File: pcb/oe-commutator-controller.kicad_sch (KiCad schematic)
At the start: 57 parts, among them J1 1719730004, U1 TEENSY-LC, U2 IS31FL3193, U3 TMC2130-LA, U4 PTN04050CAZ, U5 LTC4425

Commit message: Board revision C
- Sent to JLCPCB for testing
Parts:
- C11, C17, C6: value 2.2uF -> 4.7uF
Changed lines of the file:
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@@
       (effects (font (size 1.27 1.27)) (justify left))
     )
-    (property "Value" "2.2uF" (at 26.67 138.43 0)
+    (property "Value" "4.7uF" (at 26.67 138.43 0)
       (effects (font (size 1.27 1.27)) (justify left))
     )
@@
       (effects (font (size 1.27 1.27)) (justify left))
     )
-    (property "Value" "2.2uF" (at 151.13 41.91 0)
+    (property "Value" "4.7uF" (at 151.13 41.91 0)
       (effects (font (size 1.27 1.27)) (justify left))
     )
@@
       (effects (font (size 1.27 1.27)) (justify left))
     )
-    (property "Value" "2.2uF" (at 182.88 74.93 0)
+    (property "Value" "4.7uF" (at 182.88 74.93 0)
       (effects (font (size 1.27 1.27)) (justify left))
     )
@@
       (effects (font (size 1.27 1.27)) hide)
     )
-    (property "Datasheet" "~" (at 110.49 46.99 0)
-      (effects (font (size 1.27 1.27)) hide)
-    )
+    (property "Datasheet" "https://www.sunledusa.com/products/spec/XZMDKCBDDG45S-9.pdf" (at 110.49 46.99 0)
+      (effects (font (size 1.27 1.27)) hide)
+    )

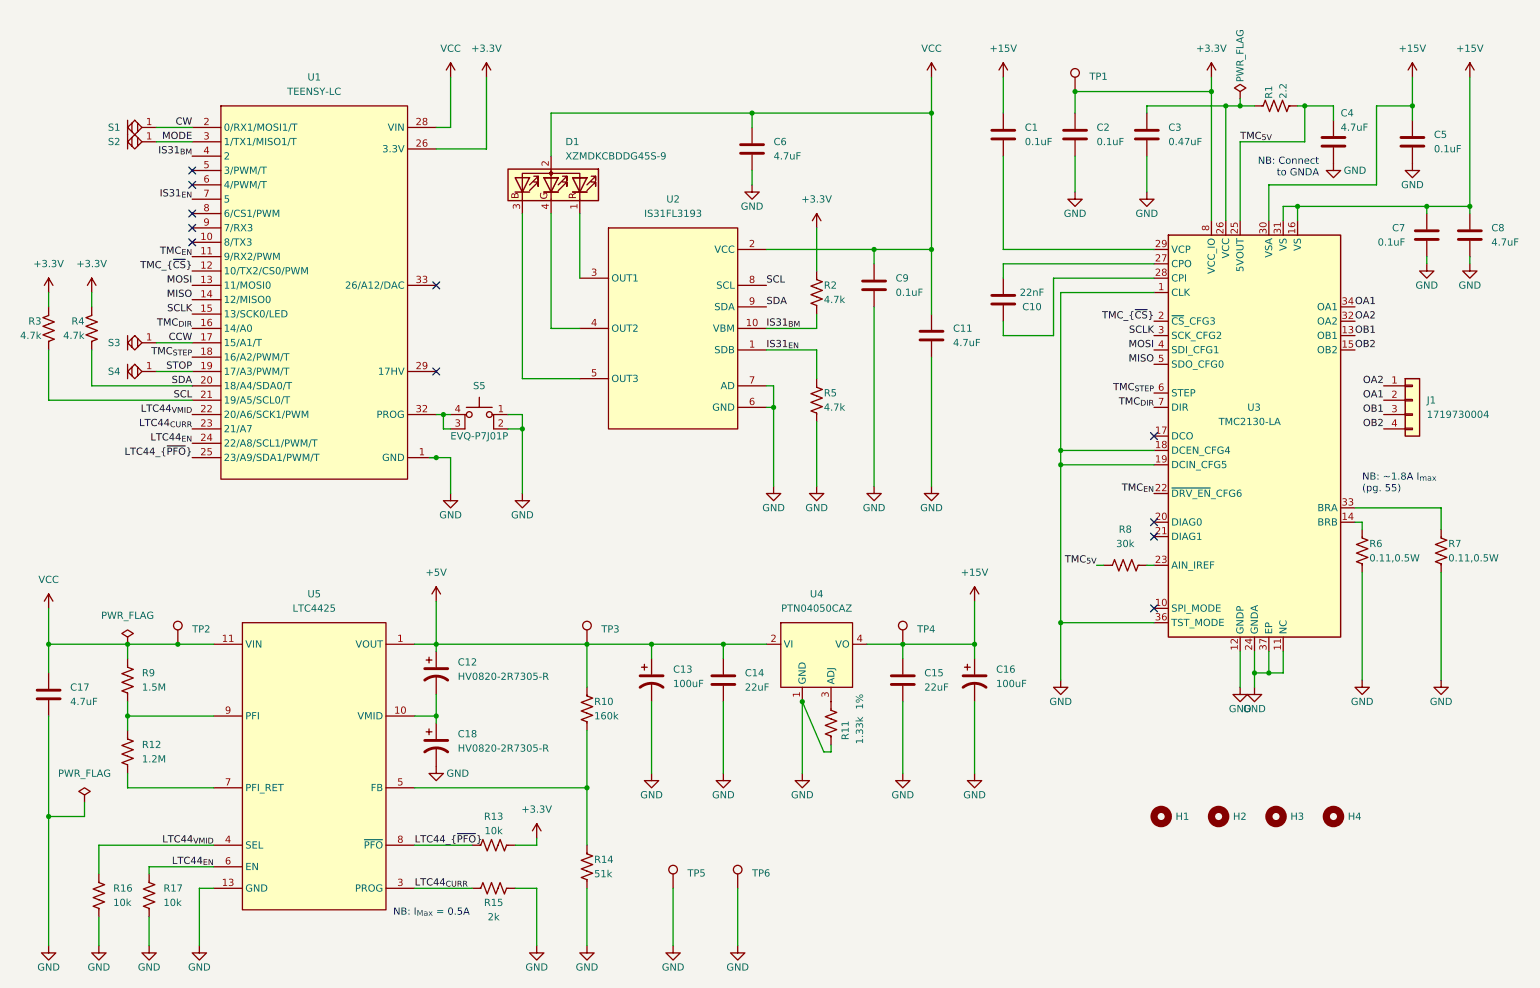
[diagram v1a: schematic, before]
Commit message: Increase R_prog to 2.49k
- This accounts for overhead current drawn from VCC by the Teensy and
  LED driver
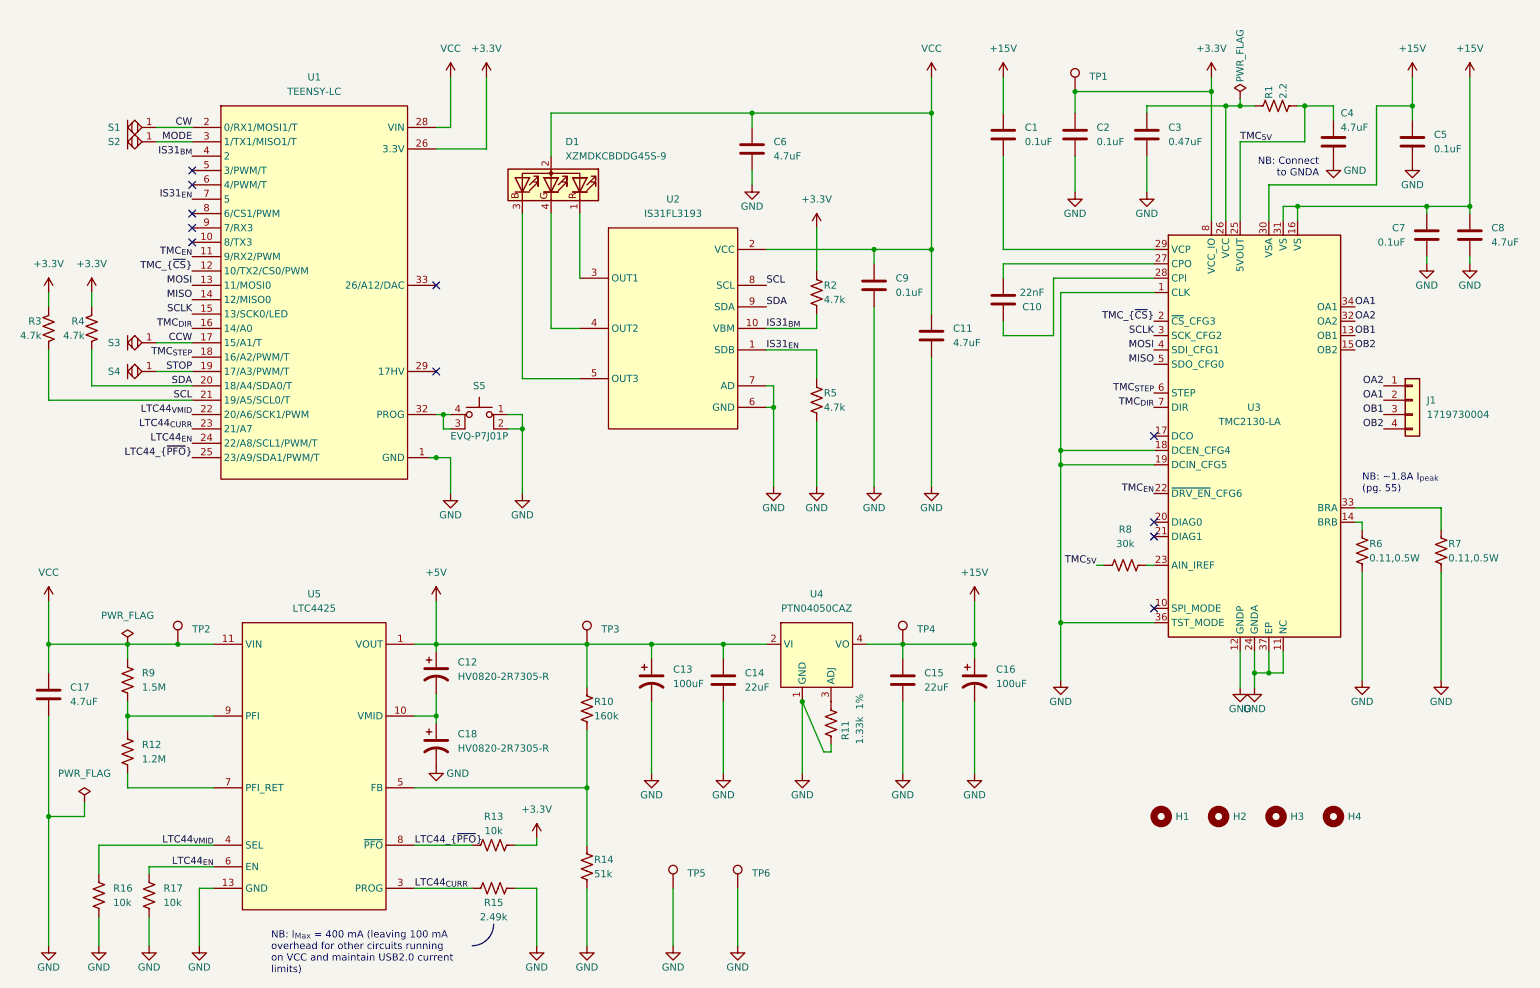
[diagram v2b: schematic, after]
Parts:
- R15: value 2k -> 2.49k
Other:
- note added: "NB: I_{Max} = 400 mA (leaving 100 mA overhead for other circuits running on VCC and maintain USB2.0 current limits)"
- note added: "NB: ~1.8A I_{peak} (pg. 55)"
- note removed: "NB: I_{Max} = 0.5A"
- note removed: "NB: ~1.8A I_{max} (pg. 55)"
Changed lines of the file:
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@@
     (stroke (width 0) (type default))
   )
-  (wire (pts (xy 22.86 121.92) (xy 22.86 128.27))
+  (wire (pts (xy 22.86 120.65) (xy 22.86 128.27))
     (stroke (width 0) (type default))
   )
@@
     (stroke (width 0) (type default))
   )
-  (text "NB: ~1.8A I_{max}\n(pg. 55)" (at 255.27 101.6 0)
+  (arc (start 101.6 177.8) (mid 100.4841 180.4941) (end 97.79 181.61)
+    (stroke (width 0) (type default))
+    (fill (type none))
+  )
+  (text "NB: ~1.8A I_{peak}\n(pg. 55)" (at 255.27 101.6 0)
     (effects (font (size 1.27 1.27)) (justify left bottom))
   )
-  (text "NB: I_{Max} = 0.5A" (at 83.82 176.53 0)
+  (text "NB: I_{Max} = 400 mA (leaving 100 mA \noverhead for other circuits running \non VCC and maintain USB2.0 current \nlimits)"
+    (at 62.23 186.69 0)
     (effects (font (size 1.27 1.27)) (justify left bottom))
   )
@@
     )
   )
-  (symbol (lib_id "power:VCC") (at 22.86 121.92 0) (unit 1)
-    (in_bom yes) (on_board yes) (dnp no) (fields_autoplaced)
-    (property "Reference" "#PWR026" (at 22.86 125.73 0)
-      (effects (font (size 1.27 1.27)) hide)
-    )
-    (property "Value" "VCC" (at 22.86 116.84 0)
-      (effects (font (size 1.27 1.27)))
-    )
-    (property "Footprint" "" (at 22.86 121.92 0)
-      (effects (font (size 1.27 1.27)) hide)
-    )
-    (property "Datasheet" "" (at 22.86 121.92 0)
+  (symbol (lib_id "power:VCC") (at 22.86 120.65 0) (unit 1)
+    (in_bom yes) (on_board yes) (dnp no) (fields_autoplaced)
+    (property "Reference" "#PWR026" (at 22.86 124.46 0)
+      (effects (font (size 1.27 1.27)) hide)
+    )
+    (property "Value" "VCC" (at 22.86 115.57 0)
+      (effects (font (size 1.27 1.27)))
+    )
+    (property "Footprint" "" (at 22.86 120.65 0)
+      (effects (font (size 1.27 1.27)) hide)
+    )
+    (property "Datasheet" "" (at 22.86 120.65 0)
       (effects (font (size 1.27 1.27)) hide)
     )
@@
       (effects (font (size 1.27 1.27)))
     )
-    (property "Value" "2k" (at 101.6 176.53 90)
-      (effects (font (size 1.27 1.27)))
-    )
+    (property "Value" "2.49k" (at 101.6 176.53 90)
+      (effects (font (size 1.27 1.27)))
+    )

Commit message: Rev D Schematic
- split schematic into several pages
- replace teensy with rp2040
- Add dedicated capacititave touch sensor ic
- Replacec Micro-Usb with USB-C
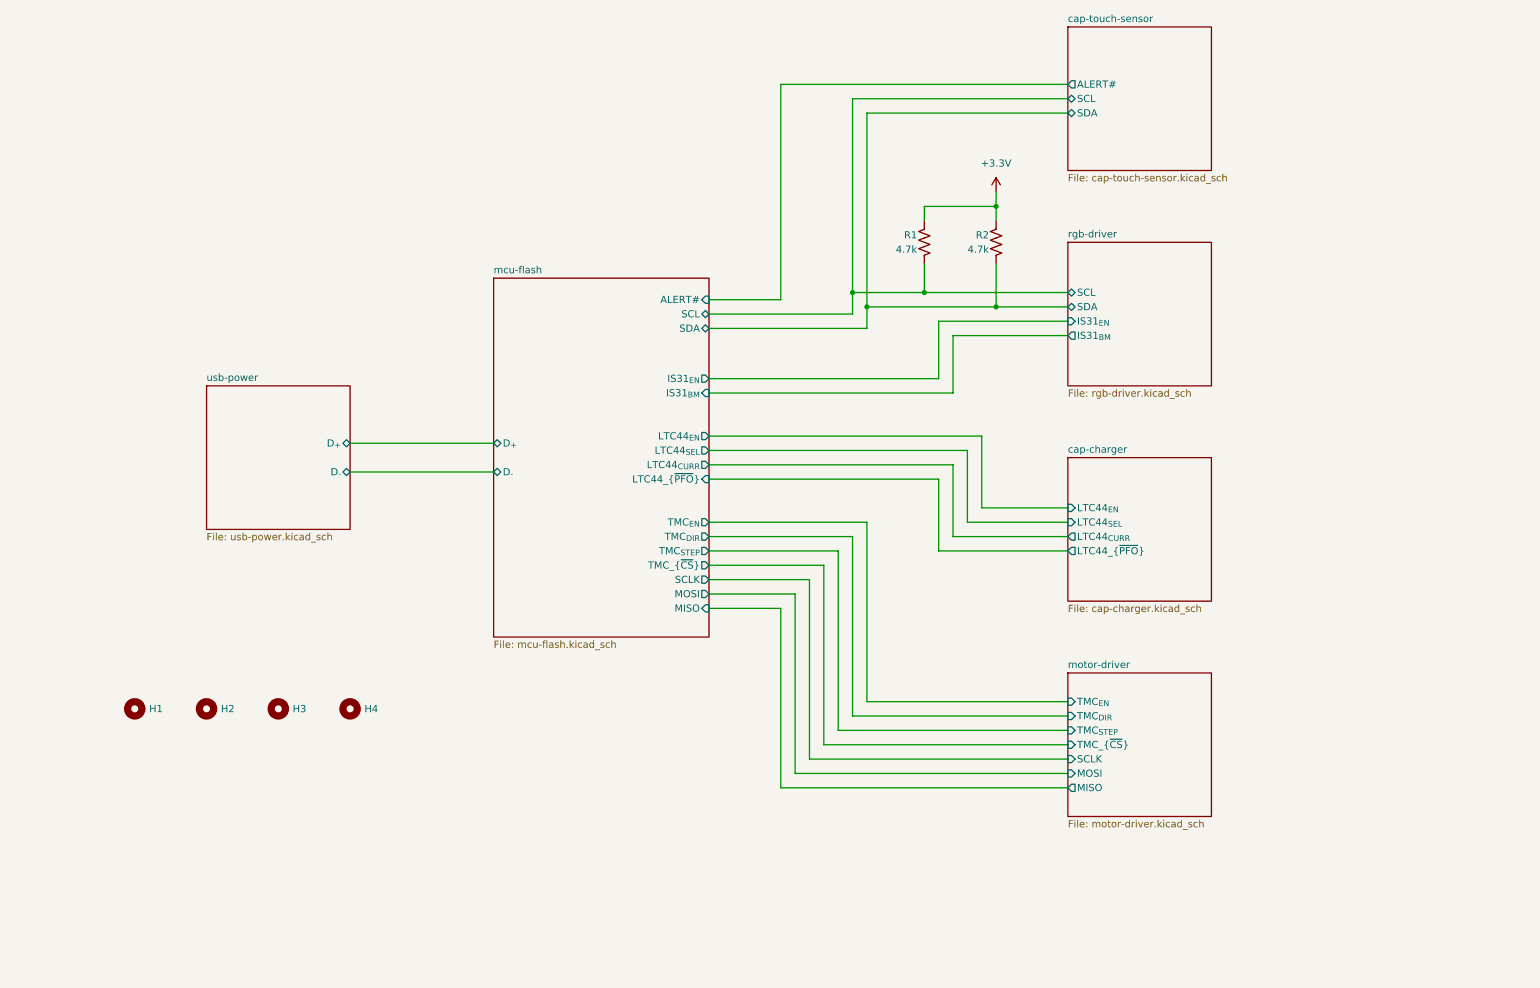
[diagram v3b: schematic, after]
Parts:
- removed C1, C2, C5, C7, C9: 0.1uF, Capacitor_SMD:C_0603_1608Metric, symbol Device:C
- removed C10: 22nF, Capacitor_SMD:C_0603_1608Metric, symbol Device:C
- removed C11, C17, C4, C6, C8: 4.7uF, Capacitor_SMD:C_0805_2012Metric, symbol Device:C
- removed C12, C18: HV0820-2R7305-R, Capacitor_SMD:C_1210_3225Metric, symbol Device:C_Polarized_US
- removed C13, C16: 100uF, Capacitor_SMD:C_Elec_8x10.2, symbol Device:C_Polarized_US
- removed C14, C15: 22uF, Capacitor_SMD:C_1206_3216Metric, symbol Device:C
- removed C3: 0.47uF, Capacitor_SMD:C_0805_2012Metric, symbol Device:C
- removed D1: XZMDKCBDDG45S-9, open-ephys:SUNLED_PLCC4-INV_3.2x2.8x1.9mm, symbol Device:LED_RABG
- removed J1: 1719730004, open-ephys:MOLEX_1719730004_1x04_P2.54mm_Vert_Lock, symbol Connector_Generic:Conn_01x04
- removed R10: 160k, Resistor_SMD:R_0603_1608Metric, symbol Device:R_US
- removed R11: 1.33k, Resistor_SMD:R_0603_1608Metric, symbol Device:R_US
- removed R12: 1.2M, Resistor_SMD:R_0603_1608Metric, symbol Device:R_US
- removed R13, R16, R17: 10k, Resistor_SMD:R_0603_1608Metric, symbol Device:R_US
- removed R14: 51k, Resistor_SMD:R_0603_1608Metric, symbol Device:R_US
- removed R15: 2.49k, Resistor_SMD:R_0603_1608Metric, symbol Device:R_US
- removed R3, R4, R5: 4.7k, Resistor_SMD:R_0603_1608Metric, symbol Device:R_US
- removed R6, R7: 0.11,0.5W, Resistor_SMD:R_1206_3216Metric, symbol Device:R_US
- removed R8: 30k, Resistor_SMD:R_0603_1608Metric, symbol Device:R_US
- removed R9: 1.5M, Resistor_SMD:R_0603_1608Metric, symbol Device:R_US
- removed S1, S2, S3, S4: ~, open-ephys:Touch_Center_2mm, symbol open-ephys:TOUCH
- removed S5: EVQ-P7J01P, open-ephys:PANASONIC_EVQP7-JA-01P, symbol Switch:SW_MEC_5E
- removed TP1, TP2, TP3, TP4, TP5, TP6: ~, TestPoint:TestPoint_Pad_D2.0mm, symbol Connector:TestPoint
- removed U1: TEENSY-LC, open-ephys:PJRC_TEENSY_SMD, symbol open-ephys:TEENSY-LC
- removed U2: IS31FL3193, Package_DFN_QFN:DFN-10-1EP_3x3mm_P0.5mm_EP1.65x2.38mm, symbol open-ephys:IS31FL3193
- removed U3: TMC2130-LA, Package_DFN_QFN:QFN-36-1EP_5x6mm_P0.5mm_EP3.6x4.1mm, symbol Driver_Motor:TMC2130-LA
- removed U4: PTN04050CAZ, open-ephys:TI_R-PDSS_B4_SMD, symbol open-ephys:PTN05050C
- removed U5: LTC4425, Package_SO:MSOP-12-1EP_3x4mm_P0.65mm_EP1.65x2.85mm, symbol open-ephys:LTC4425
- R1: value 2.2 -> 4.7k
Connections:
- net +3.3V: now also R1.1
- net IS31_{BM} renamed cap-touch-sensor/SDA
- net TMC_{5V} renamed cap-touch-sensor/SCL
- no-connect marks 11 -> 0
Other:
- added sheet cap-charger (cap-charger.kicad_sch)
- added sheet cap-touch-sensor (cap-touch-sensor.kicad_sch)
- added sheet mcu-flash (mcu-flash.kicad_sch)
- added sheet motor-driver (motor-driver.kicad_sch)
- added sheet rgb-driver (rgb-driver.kicad_sch)
- added sheet usb-power (usb-power.kicad_sch)
- note removed: "NB: Connect to GNDA"
- note removed: "NB: I_{Max} = 400 mA (leaving 100 mA overhead for other circuits running on VCC and maintain USB2.0 current limits)"
- note removed: "NB: ~1.8A I_{peak} (pg. 55)"
- moved on the sheet: H1, H2, H3, H4

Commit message: Replaced through-hole components with SMD
- Other small edits (e.g. optional jumper to force USB-boot)
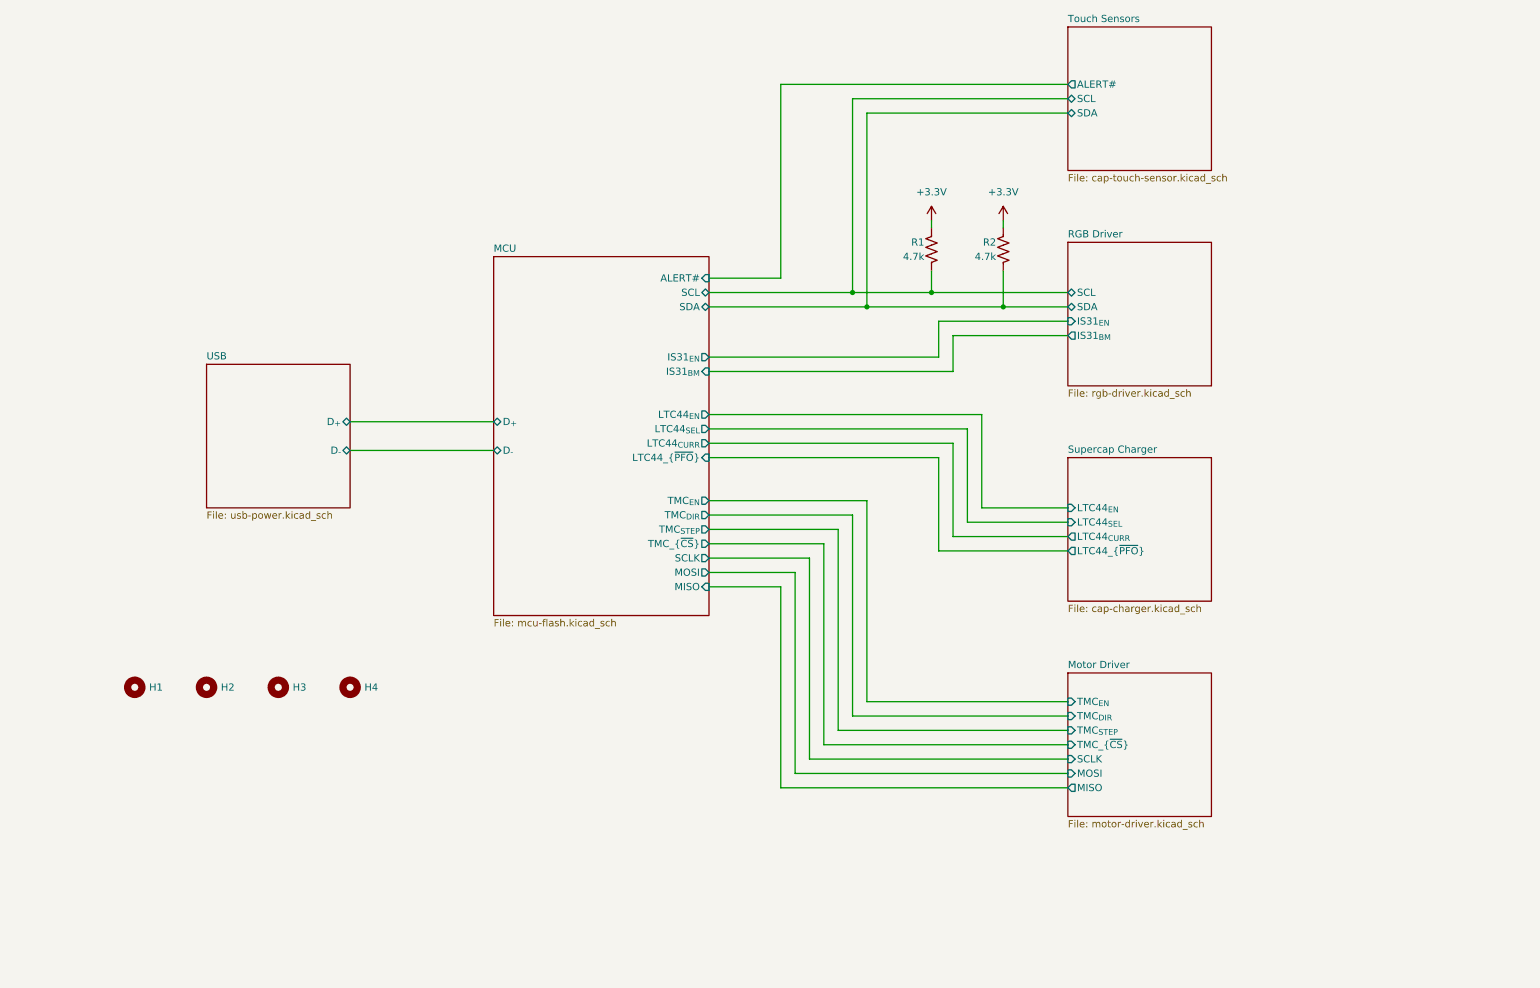
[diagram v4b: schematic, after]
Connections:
- net Touch Sensors/SCL renamed MCU/SCL
- net Touch Sensors/SDA renamed MCU/SDA
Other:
- sheet cap-charger renamed Supercap Charger
- sheet cap-touch-sensor renamed Touch Sensors
- sheet mcu-flash renamed MCU
- sheet motor-driver renamed Motor Driver
- sheet rgb-driver renamed RGB Driver
- sheet usb-power renamed USB
- moved on the sheet: H1, H2, H3, H4
